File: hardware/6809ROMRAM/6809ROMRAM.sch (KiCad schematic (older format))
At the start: 10 parts, among them J1 SS50-LIKE, J2 Address Select, U1 628128, U2 28C256, U3 28C256, U4 74HC85

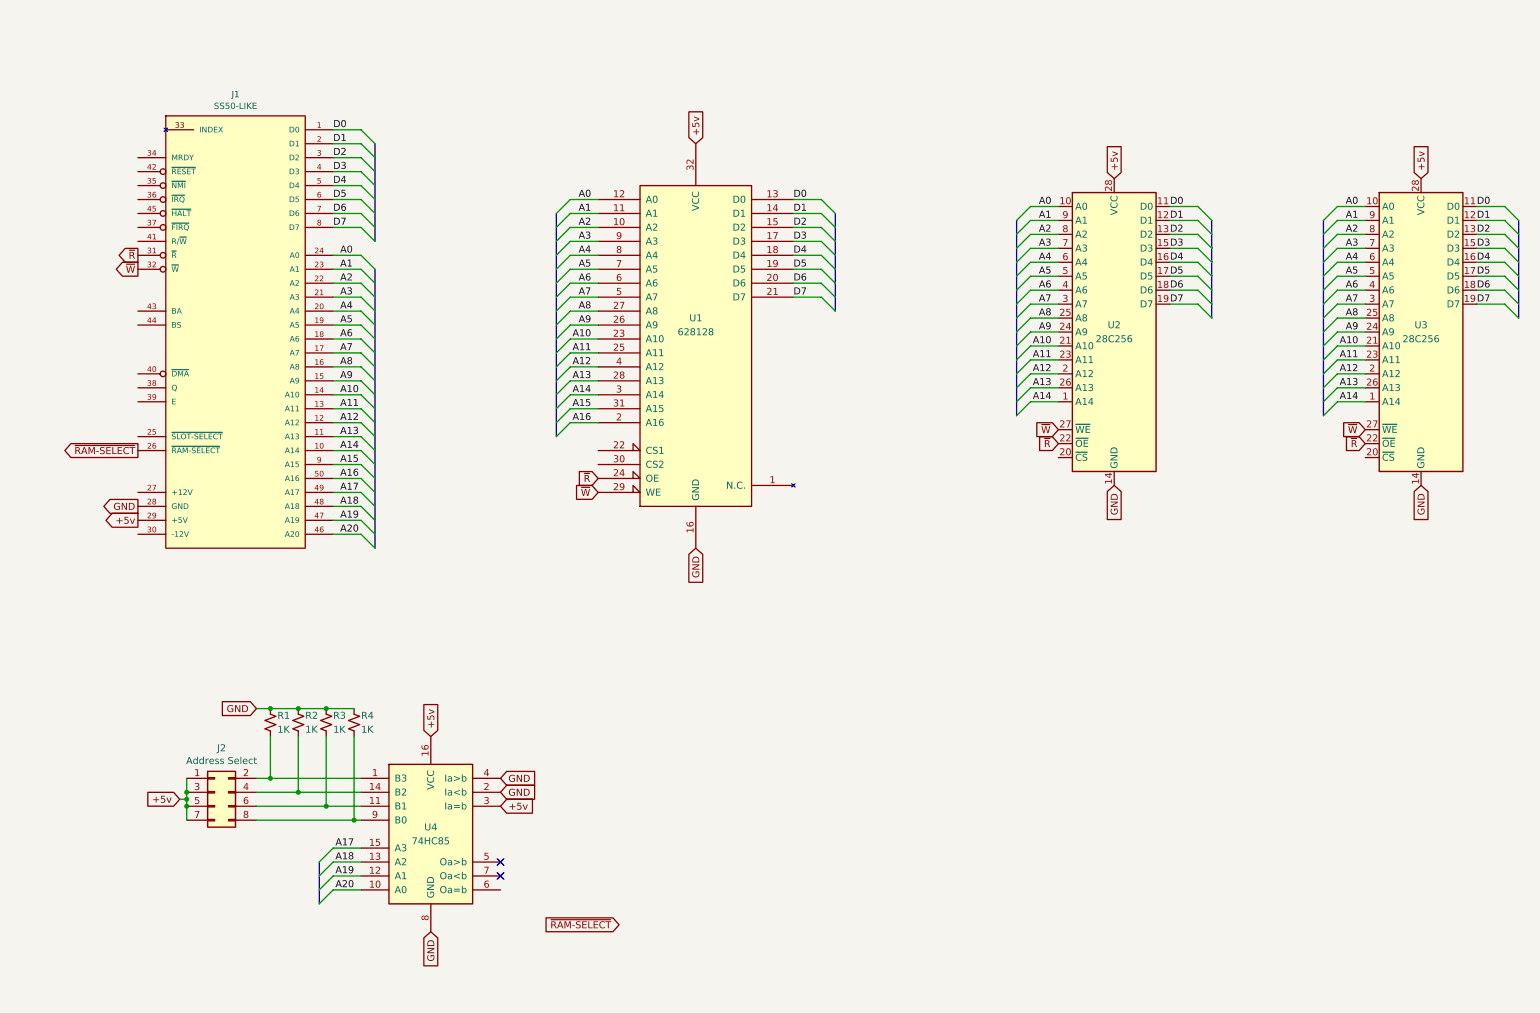
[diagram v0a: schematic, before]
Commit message: schematic for ROM/RAM card
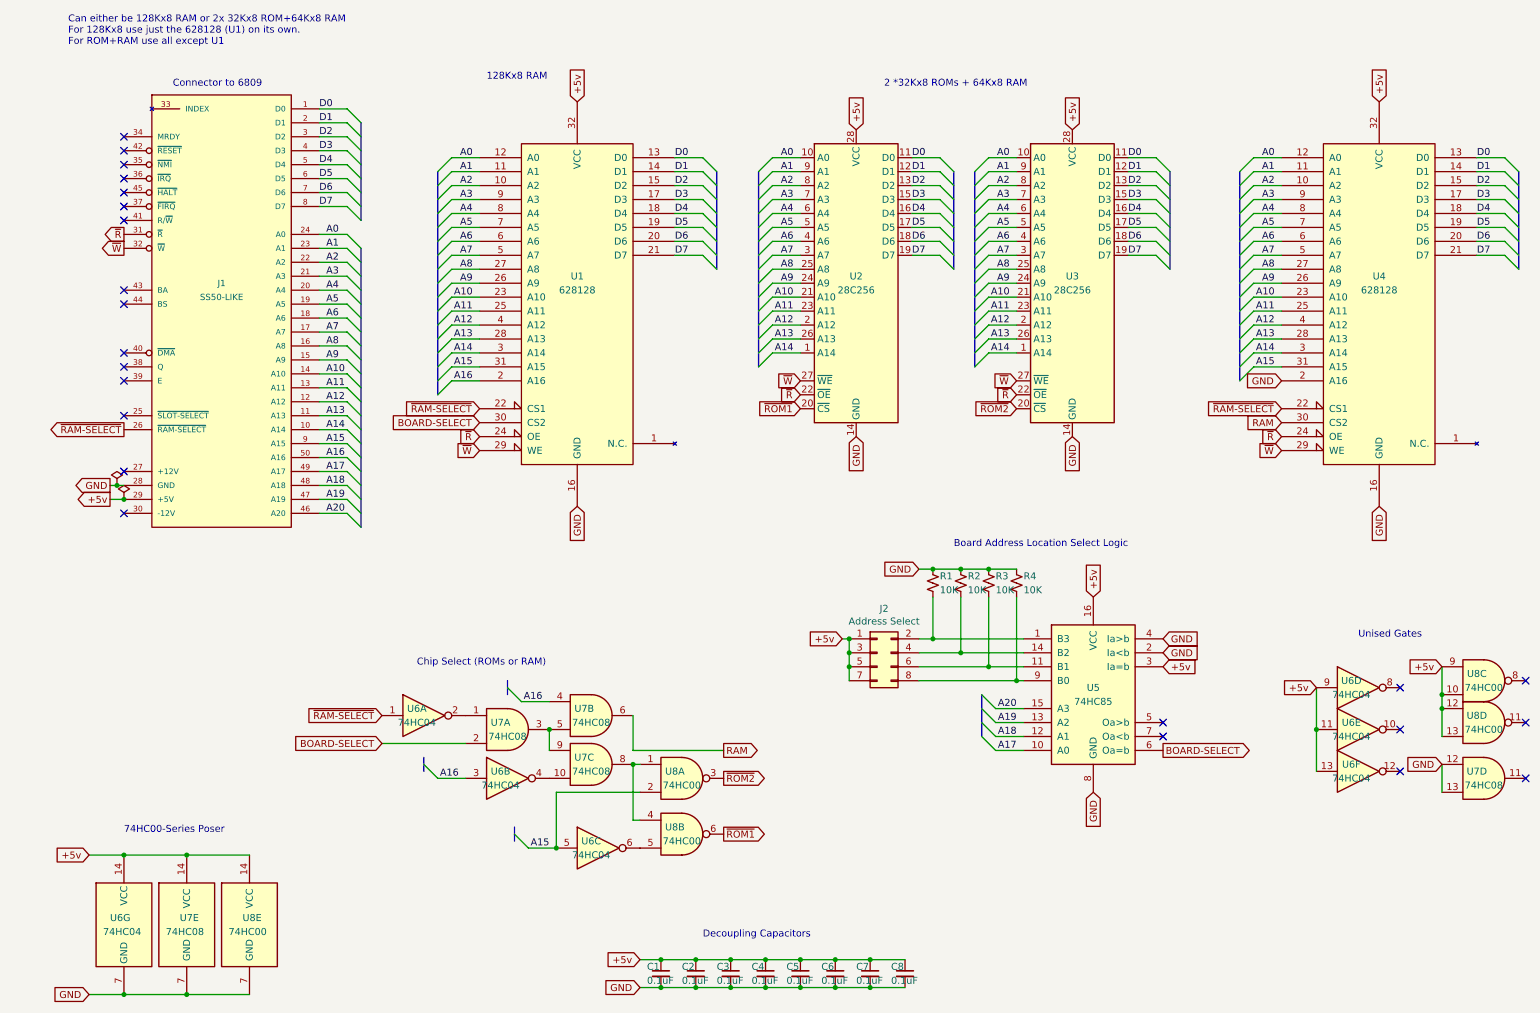
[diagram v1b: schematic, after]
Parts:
- added C1, C2, C3, C4, C5, C6, C7, C8: 0.1uF, Capacitor_THT:C_Disc_D5.0mm_W2.5mm_P5.00mm, symbol Device:C_Small
- added U4: 628128, Package_DIP:DIP-32_W15.24mm_Socket_LongPads, symbol aspt:628128
- added U6: 74HC04, Package_DIP:DIP-14_W7.62mm_LongPads, symbol 74xx:74HC04
- added U7: 74HC08, Package_DIP:DIP-14_W7.62mm_LongPads, symbol 74xx:74LS08
- added U8: 74HC00, Package_DIP:DIP-14_W7.62mm_LongPads, symbol 74xx:74HC00
- J1: footprint SS-50_SS-50_BOARD_CONNECTOR -> Connector_PinHeader_2.54mm:PinHeader_2x25_P2.54mm_Vertical
- J2: footprint (none) -> Connector_PinHeader_2.54mm:PinHeader_2x04_P2.54mm_Vertical
- R1, R2, R3, R4: value 1K -> 10K; footprint (none) -> Resistor_THT:R_Axial_DIN0309_L9.0mm_D3.2mm_P12.70mm_Horizontal
- U1: footprint (none) -> Package_DIP:DIP-32_W15.24mm_Socket_LongPads
- U2, U3: footprint (none) -> Package_DIP:DIP-28_W15.24mm_Socket_LongPads
- U5: renamed from U4; footprint (none) -> Package_DIP:DIP-16_W7.62mm_LongPads
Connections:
- net +5v: now also C1.1, C2.1, C3.1, C4.1, C5.1, C6.1, C7.1, C8.1, U4.32 (VCC), U6.11, U6.13, U6.14 (VCC), U6.9, U7.14 (VCC), U8.10, U8.12, U8.13, U8.14 (VCC), U8.9
- net A0: now also U4.12 (A0)
- net A1: now also U4.11 (A1)
- net A10: now also U4.23 (A10)
- net A11: now also U4.25 (A11)
- net A12: now also U4.4 (A12)
- net A13: now also U4.28 (A13)
- net A14: now also U4.3 (A14)
- net A15: now also U4.31 (A15), U6.5, U8.2
- net A16: now also U6.3, U7.4
- net A17: now also U5.10 (A0); no longer U5.15 (A3)
- net A18: now also U5.12 (A1); no longer U5.13 (A2)
- net A19: now also U5.13 (A2); no longer U5.12 (A1)
- net A2: now also U4.10 (A2)
- net A20: now also U5.15 (A3); no longer U5.10 (A0)
- net A3: now also U4.9 (A3)
- net A4: now also U4.8 (A4)
- net A5: now also U4.7 (A5)
- net A6: now also U4.6 (A6)
- net A7: now also U4.5 (A7)
- net A8: now also U4.27 (A8)
- net A9: now also U4.26 (A9)
- net D0: now also U4.13 (D0)
- net D1: now also U4.14 (D1)
- net D2: now also U4.15 (D2)
- net D3: now also U4.17 (D3)
- net D4: now also U4.18 (D4)
- net D5: now also U4.19 (D5)
- net D6: now also U4.20 (D6)
- net D7: now also U4.21 (D7)
- net GND: now also C1.2, C2.2, C3.2, C4.2, C5.2, C6.2, C7.2, C8.2, U4.16 (GND), U4.2 (A16), U6.7 (GND), U7.12, U7.13, U7.7 (GND), U8.7 (GND)
- net ~R: now also U4.24 (OE)
- net ~RAM-SELECT: now also U1.22 (CS1), U4.22 (CS1), U6.1
- net ~W: now also U4.29 (WE)
- net BOARD-SELECT: now reaches U1.30 (CS2)
- net BOARD-SELECT: now also U5.6 (Oa=b), U7.2
- net ~ROM1: now reaches U2.20 (~CS)
- net ~ROM1: now also U8.6
- net ~ROM2: now reaches U3.20 (~CS)
- net ~ROM2: now also U8.3
- new net: U6.2, U7.1
- new net: U7.3, U7.5, U7.9
- new net: U6.4, U7.10
- new net: U7.8, U8.1, U8.4
- new net: U6.6, U8.5
- new net RAM: U4.30 (CS2), U7.6
- no-connect marks 2 -> 23
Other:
- note added: "128Kx8 RAM"
- note added: "2 *32Kx8 ROMs + 64Kx8 RAM"
- note added: "74HC00-Series Poser"
- note added: "Board Address Location Select Logic"
- note added: "Can either be 128Kx8 RAM or 2x 32Kx8 ROM+64Kx8 RAM\nFor 128Kx8 use just the 628128 (U1) on its own.\nFor ROM+RAM use all except U1"
- note added: "Chip Select (ROMs or RAM)"
- note added: "Connector to 6809"
- note added: "Decoupling Capacitors"
- note added: "Unised Gates"
- moved on the sheet: J1, J2, R1, R2, R3, R4, U1, U2, U3, U5

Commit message: ROMRAM board
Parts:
- added H1, H2, H3, H4: MountingHole, MountingHole:MountingHole_3.2mm_M3_ISO14580_Pad, symbol Mechanical:MountingHole
- added Logo1: Pinnated, Pinnated:Pinnule, symbol aspt:Pinnated
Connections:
- net +5v: now also C2.2, C3.2, C4.2, C5.2, C6.2, C7.2, C8.2; no longer C2.1, C3.1, C4.1, C5.1, C6.1, C7.1, C8.1
- net GND: now also C2.1, C3.1, C4.1, C5.1, C6.1, C7.1, C8.1; no longer C2.2, C3.2, C4.2, C5.2, C6.2, C7.2, C8.2
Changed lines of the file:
@@
 F 3 "~" H 5150 7550 50  0001 C CNN
 	1    5150 7550
-	1    0    0    -1
+	-1   0    0    1
 $EndComp
 $Comp
@@
 F 3 "~" H 5400 7550 50  0001 C CNN
 	1    5400 7550
-	1    0    0    -1
+	-1   0    0    1
 $EndComp
 $Comp
@@
 F 3 "~" H 5650 7550 50  0001 C CNN
 	1    5650 7550
-	1    0    0    -1
-$EndComp
-$Comp
-L Device:C_Small C5
-U 1 1 6115D68F
-P 5900 7550
-F 0 "C5" H 5800 7600 50  0000 L CNN
-F 1 "0.1uF" H 5800 7500 50  0000 L CNN
-F 2 "Capacitor_THT:C_Disc_D5.0mm_W2.5mm_P5.00mm" H 5900 7550 50  0001 C CNN
-F 3 "~" H 5900 7550 50  0001 C CNN
-	1    5900 7550
-	1    0    0    -1
+	-1   0    0    1
 $EndComp
 $Comp
@@
 F 3 "~" H 6150 7550 50  0001 C CNN
 	1    6150 7550
-	1    0    0    -1
+	-1   0    0    1
 $EndComp
 $Comp
@@
 F 3 "~" H 6400 7550 50  0001 C CNN
 	1    6400 7550
-	1    0    0    -1
+	-1   0    0    1
 $EndComp
 Wire Wire Line
@@
 Wire Wire Line
 	5650 7450 5400 7450
-Connection ~ 5900 7450
-Wire Wire Line
-	5900 7450 5650 7450
 Connection ~ 6150 7450
-Wire Wire Line
-	6150 7450 5900 7450
 Wire Wire Line
 	4900 7650 5150 7650
@@
 	5400 7650 5650 7650
 Connection ~ 5650 7650
-Wire Wire Line
-	5650 7650 5900 7650
-Connection ~ 5900 7650
-Wire Wire Line
-	5900 7650 6150 7650
 Connection ~ 6150 7650
 Wire Wire Line
@@
 F 3 "~" H 6650 7550 50  0001 C CNN
 	1    6650 7550
-	1    0    0    -1
+	-1   0    0    1
 $EndComp
 Wire Wire Line
@@
 Text Notes 650  900  0    50   ~ 0
 Can either be 128Kx8 RAM or 2x 32Kx8 ROM+64Kx8 RAM\nFor 128Kx8 use just the 628128 (U1) on its own.\nFor ROM+RAM use all except U1
+$Comp
+L aspt:Pinnated Logo1
+U 1 1 6085CEAD
+P 2900 7450
+F 0 "Logo1" H 2925 7496 50  0001 L CNN
+F 1 "Pinnated" H 2925 7405 50  0000 L CNN
+F 2 "Pinnated:Pinnule" H 2900 7450 50  0001 C CNN
+F 3 "" H 2900 7450 50  0001 C CNN
+	1    2900 7450
+	1    0    0    -1
+$EndComp
+$Comp
+L Mechanical:MountingHole H3
+U 1 1 608AEDA7
+P 3050 7200
+F 0 "H3" H 3150 7200 50  0000 L CNN
+F 1 "MountingHole" H 3150 7155 50  0001 L CNN
+F 2 "MountingHole:MountingHole_3.2mm_M3_ISO14580_Pad" H 3050 7200 50  0001 C CNN
+F 3 "~" H 3050 7200 50  0001 C CNN
+	1    3050 7200
+	1    0    0    -1
+$EndComp
+$Comp
+L Mechanical:MountingHole H4
+U 1 1 608B0027
+P 3050 7350
+F 0 "H4" H 3150 7350 50  0000 L CNN
+F 1 "MountingHole" H 3150 7305 50  0001 L CNN
+F 2 "MountingHole:MountingHole_3.2mm_M3_ISO14580_Pad" H 3050 7350 50  0001 C CNN
+F 3 "~" H 3050 7350 50  0001 C CNN
+	1    3050 7350
+	1    0    0    -1
+$EndComp
+$Comp
+L Mechanical:MountingHole H2
+U 1 1 608C2F83
+P 3050 7050
+F 0 "H2" H 3150 7050 50  0000 L CNN
+F 1 "MountingHole" H 3150 7005 50  0001 L CNN
+F 2 "MountingHole:MountingHole_3.2mm_M3_ISO14580_Pad" H 3050 7050 50  0001 C CNN
+F 3 "~" H 3050 7050 50  0001 C CNN
+	1    3050 7050
+	1    0    0    -1
+$EndComp
+$Comp
+L Mechanical:MountingHole H1
+U 1 1 608D5285
+P 3050 6900
+F 0 "H1" H 3150 6900 50  0000 L CNN
+F 1 "MountingHole" H 3150 6855 50  0001 L CNN
+F 2 "MountingHole:MountingHole_3.2mm_M3_ISO14580_Pad" H 3050 6900 50  0001 C CNN
+F 3 "~" H 3050 6900 50  0001 C CNN
+	1    3050 6900
+	1    0    0    -1
+$EndComp
+Connection ~ 5900 7650
+Wire Wire Line
+	5900 7650 6150 7650
+Wire Wire Line
+	5650 7650 5900 7650
+Wire Wire Line
+	6150 7450 5900 7450
+Wire Wire Line
+	5900 7450 5650 7450
+Connection ~ 5900 7450
+$Comp
+L Device:C_Small C5
+U 1 1 6115D68F
+P 5900 7550
+F 0 "C5" H 5800 7600 50  0000 L CNN
+F 1 "0.1uF" H 5800 7500 50  0000 L CNN
+F 2 "Capacitor_THT:C_Disc_D5.0mm_W2.5mm_P5.00mm" H 5900 7550 50  0001 C CNN
+F 3 "~" H 5900 7550 50  0001 C CNN
+	1    5900 7550
+	-1   0    0    1
+$EndComp
 Wire Bus Line
 	3850 6500 3850 6600
